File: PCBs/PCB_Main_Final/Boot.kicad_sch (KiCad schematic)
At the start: 12 parts, among them SW5 SW_Push, SW6 SW_Push, SW7 SW_Push, SW8 SW_Push

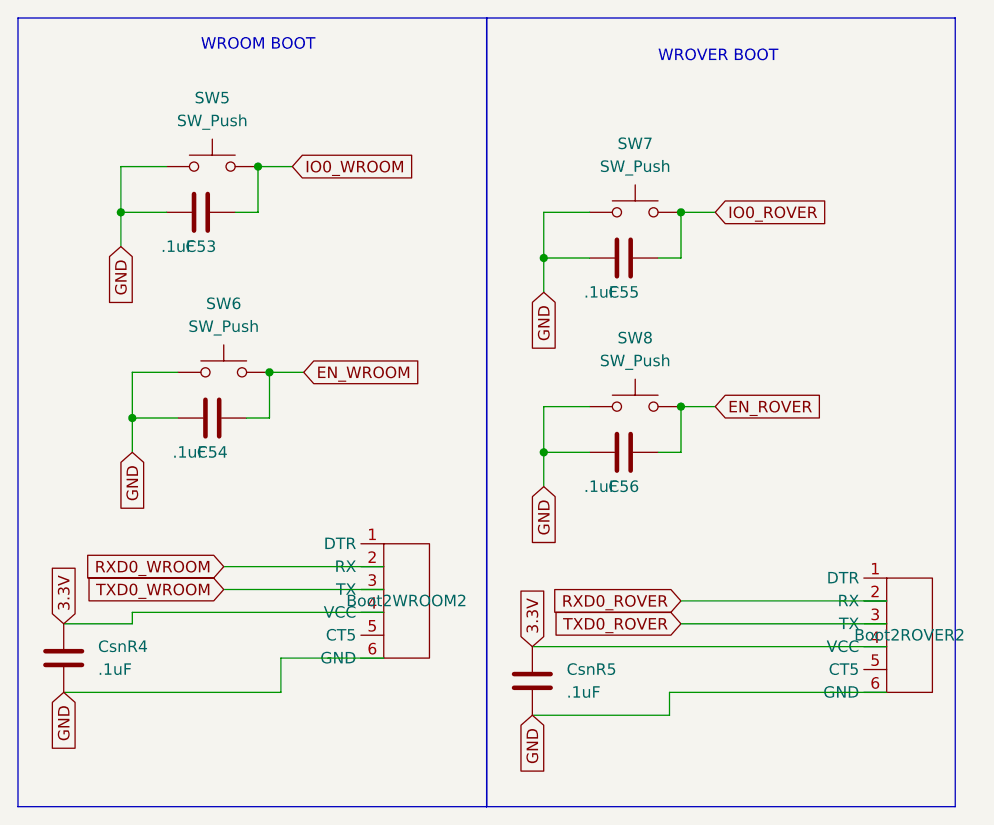
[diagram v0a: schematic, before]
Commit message: finished Main and Light Sensor PCBs
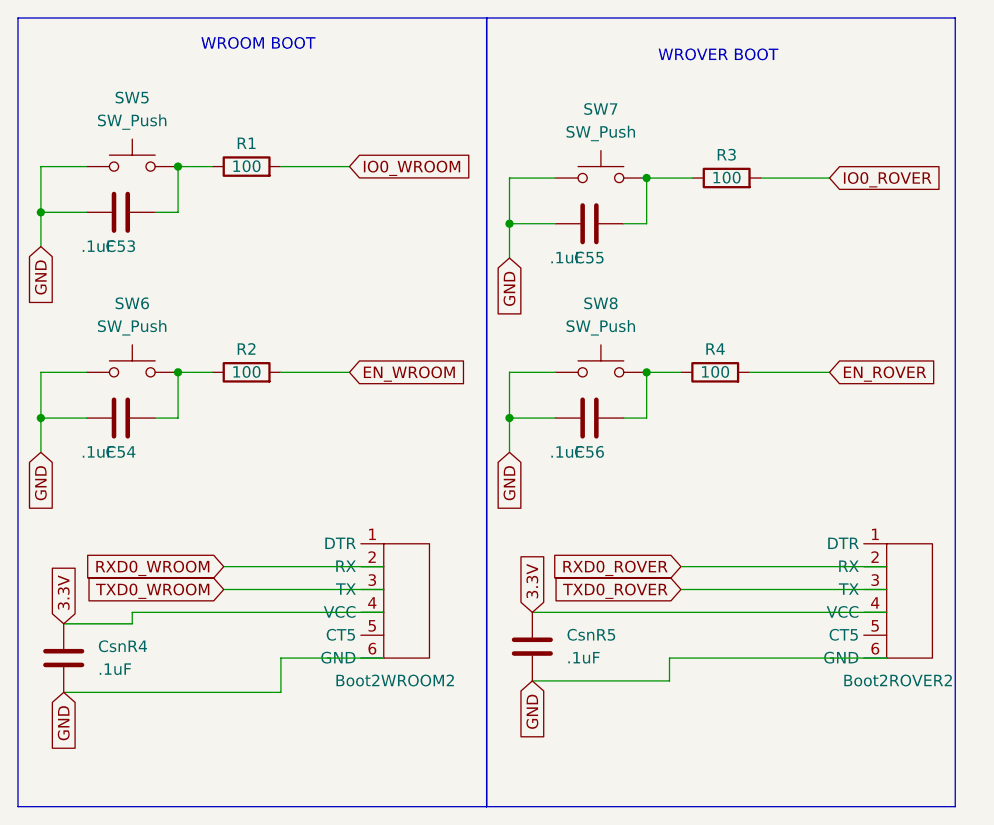
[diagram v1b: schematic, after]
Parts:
- added R1, R2, R3, R4: 100, Resistor_SMD:R_0805_2012Metric, symbol Device:R
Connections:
- net EN_ROVER: now also R4.2; no longer C56.2, SW8.2
- net EN_WROOM: now also R2.2; no longer C54.2, SW6.2
- net IO0_ROVER: now also R3.2; no longer C55.2, SW7.2
- net IO0_WROOM: now also R1.2; no longer C53.2, SW5.2
- new net: C55.2, R3.1, SW7.2
- new net: C54.2, R2.1, SW6.2
- new net: C53.2, R1.1, SW5.2
- new net: C56.2, R4.1, SW8.2
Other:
- moved on the sheet: Boot2ROVER2, C53, C54, C55, C56, CsnR5, SW5, SW6, SW7, SW8
